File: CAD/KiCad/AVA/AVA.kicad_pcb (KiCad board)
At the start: 2 copper layers, 100 x 75 mm, 48 parts, among them J1 Conn_01x03_Pin, J10 Conn_01x04_Pin, J2 Conn_01x03_Pin, J3 Conn_01x03_Pin, J4 Conn_01x03_Pin, J5 Conn_01x02_Pin, J6 Conn_01x02_Pin, J7 Conn_01x02_Pin, J8 Conn_01x03_Pin, J9 Conn_01x03_Pin, U1 ESP32-C3-Super-Mini, U2 ESP32-DevKitC

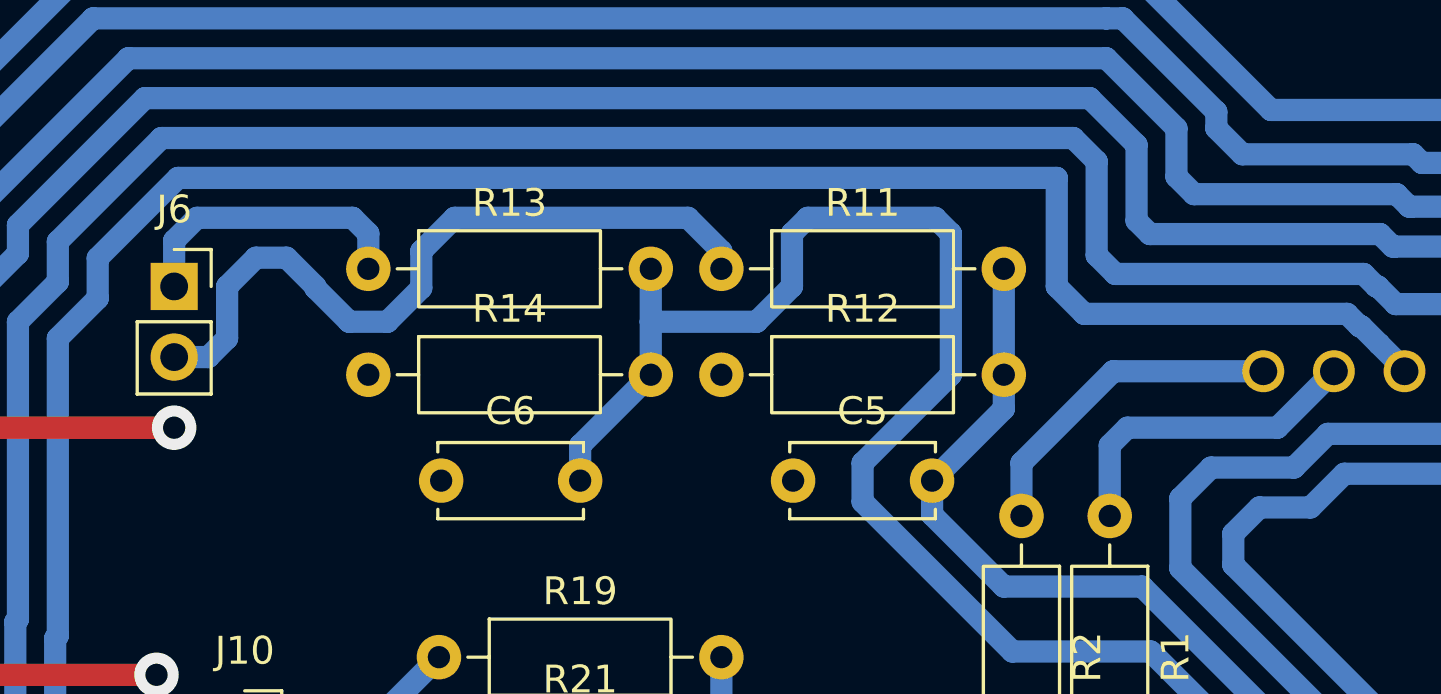
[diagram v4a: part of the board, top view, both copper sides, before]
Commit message: Added edges to Cu-Edit
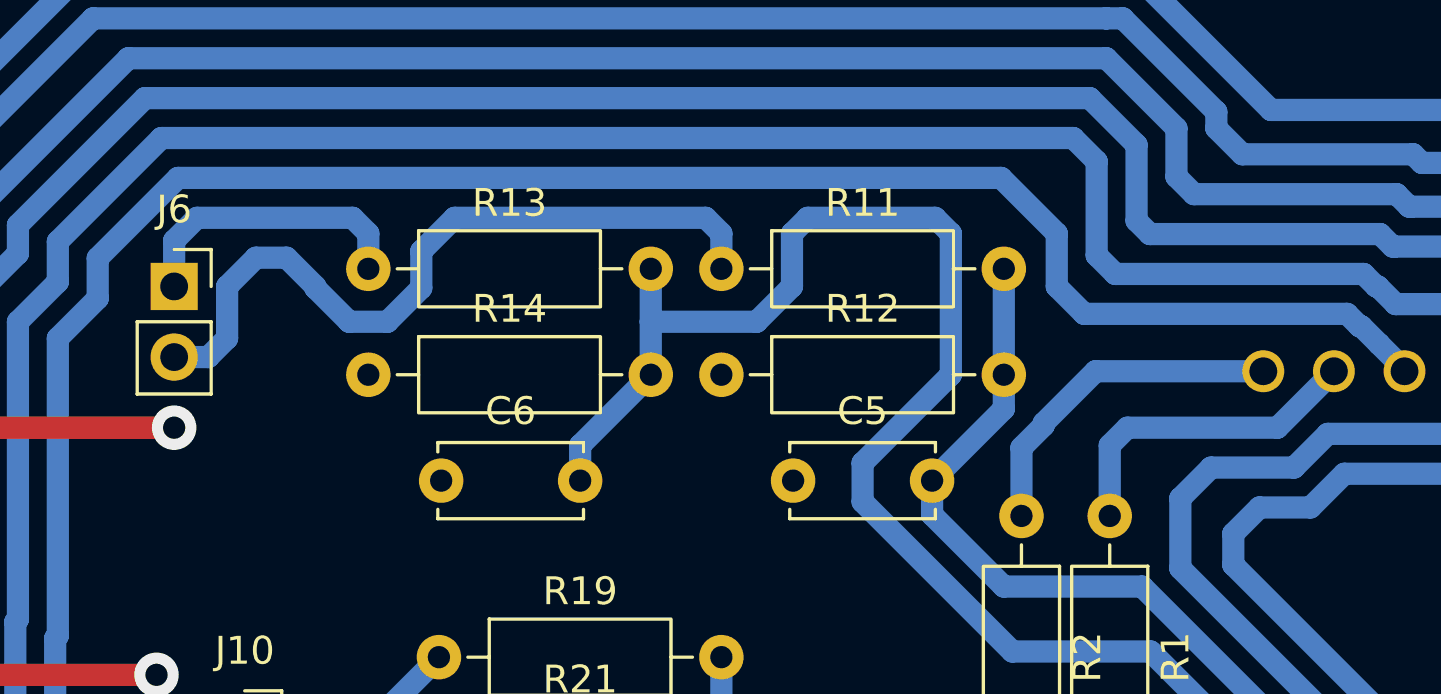
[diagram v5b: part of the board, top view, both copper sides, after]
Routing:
- net Net-(U1-GPIO10): track 88.1 -> 86.9 mm
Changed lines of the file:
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@@
+	)
+	(segment
+		(start 192.405 61.595)
+		(end 192.405 63.5)
+		(width 0.8)
+		(layer "B.Cu")
+		(net "Net-(U1-GPIO10)")
+	)
+	(segment
+		(start 203.999999 65.569999)
+		(end 204.915 66.485)
+		(width 0.8)
+		(layer "B.Cu")
+		(net "Net-(U1-GPIO10)")
+	)
+	(segment
+		(start 156.47 65.364396)
+		(end 157.904998 63.929398)
+		(width 0.8)
+		(layer "B.Cu")
+		(net "Net-(U1-GPIO10)")
+	)
+	(segment
+		(start 151.765 94.615)
+		(end 153.732198 92.647802)
+		(width 0.8)
+		(layer "B.Cu")
+		(net "Net-(U1-GPIO10)")
+	)
+	(segment
+		(start 202.85 64.485)
+		(end 203.3 64.935)
+		(width 0.8)
+		(layer "B.Cu")
+		(net "Net-(U1-GPIO10)")
+	)
+	(segment
+		(start 157.904998 63.929398)
+		(end 157.904998 62.480002)
+		(width 0.8)
+		(layer "B.Cu")
+		(net "Net-(U1-GPIO10)")
+	)
+	(segment
+		(start 156.375 76.159396)
+		(end 156.469999 76.064397)
+		(width 0.8)
+		(layer "B.Cu")
+		(net "Net-(U1-GPIO10)")
 	)
 	(segment
@@
 	)
 	(segment
+		(start 153.732198 92.647802)
+		(end 153.732198 85.787198)
+		(width 0.8)
+		(layer "B.Cu")
+		(net "Net-(U1-GPIO10)")
+	)
+	(segment
 		(start 160.79 59.595)
-		(end 192.405 59.595)
-		(width 0.8)
-		(layer "B.Cu")
-		(net "Net-(U1-GPIO10)")
-	)
-	(segment
-		(start 157.904998 63.929398)
-		(end 157.904998 62.480002)
-		(width 0.8)
-		(layer "B.Cu")
-		(net "Net-(U1-GPIO10)")
-	)
-	(segment
-		(start 203.999999 65.569999)
-		(end 204.915 66.485)
-		(width 0.8)
-		(layer "B.Cu")
-		(net "Net-(U1-GPIO10)")
-	)
-	(segment
-		(start 151.765 94.615)
-		(end 153.732198 92.647802)
+		(end 190.405 59.595)
+		(width 0.8)
+		(layer "B.Cu")
+		(net "Net-(U1-GPIO10)")
+	)
+	(segment
+		(start 190.405 59.595)
+		(end 192.405 61.595)
+		(width 0.8)
+		(layer "B.Cu")
+		(net "Net-(U1-GPIO10)")
+	)
+	(segment
+		(start 204.915 66.485)
+		(end 204.915 66.55)
+		(width 0.8)
+		(layer "B.Cu")
+		(net "Net-(U1-GPIO10)")
+	)
+	(segment
+		(start 192.405 63.5)
+		(end 193.39 64.485)
+		(width 0.8)
+		(layer "B.Cu")
+		(net "Net-(U1-GPIO10)")
+	)
+	(segment
+		(start 203.3 64.935)
+		(end 203.364986 64.934999)
+		(width 0.8)
+		(layer "B.Cu")
+		(net "Net-(U1-GPIO10)")
+	)
+	(segment
+		(start 156.375 83.144396)
+		(end 156.375 76.159396)
+		(width 0.8)
+		(layer "B.Cu")
+		(net "Net-(U1-GPIO10)")
+	)
+	(segment
+		(start 203.364986 64.934999)
+		(end 203.999987 65.57)
+		(width 0.8)
+		(layer "B.Cu")
+		(net "Net-(U1-GPIO10)")
+	)
+	(segment
+		(start 157.904998 62.480002)
+		(end 160.79 59.595)
+		(width 0.8)
+		(layer "B.Cu")
+		(net "Net-(U1-GPIO10)")
+	)
+	(segment
+		(start 203.999987 65.57)
+		(end 203.999999 65.569999)
 		(width 0.8)
 		(layer "B.Cu")
@@
 	)
 	(segment
-		(start 153.732198 92.647802)
-		(end 153.732198 85.787198)
-		(width 0.8)
-		(layer "B.Cu")
-		(net "Net-(U1-GPIO10)")
-	)
-	(segment
-		(start 203.364986 64.934999)
-		(end 203.999987 65.57)
-		(width 0.8)
-		(layer "B.Cu")
-		(net "Net-(U1-GPIO10)")
-	)
-	(segment
-		(start 203.999987 65.57)
-		(end 203.999999 65.569999)
-		(width 0.8)
-		(layer "B.Cu")
-		(net "Net-(U1-GPIO10)")
-	)
-	(segment
 		(start 156.469999 76.064397)
 		(end 156.47 65.364396)
@@
 	)
 	(segment
-		(start 156.47 65.364396)
-		(end 157.904998 63.929398)
-		(width 0.8)
-		(layer "B.Cu")
-		(net "Net-(U1-GPIO10)")
-	)
-	(segment
-		(start 203.3 64.935)
-		(end 203.364986 64.934999)
-		(width 0.8)
-		(layer "B.Cu")
-		(net "Net-(U1-GPIO10)")
-	)
-	(segment
-		(start 156.375 76.159396)
-		(end 156.469999 76.064397)
-		(width 0.8)
-		(layer "B.Cu")
-		(net "Net-(U1-GPIO10)")
-	)
-	(segment
-		(start 204.915 66.485)
-		(end 204.915 66.55)
-		(width 0.8)
-		(layer "B.Cu")
-		(net "Net-(U1-GPIO10)")
-	)
-	(segment
-		(start 157.904998 62.480002)
-		(end 160.79 59.595)
-		(width 0.8)
-		(layer "B.Cu")
-		(net "Net-(U1-GPIO10)")
-	)
-	(segment
-		(start 192.405 59.595)
-		(end 192.405 63.5)
-		(width 0.8)
-		(layer "B.Cu")
-		(net "Net-(U1-GPIO10)")
-	)
-	(segment
-		(start 192.405 63.5)
-		(end 193.39 64.485)
-		(width 0.8)
-		(layer "B.Cu")
-		(net "Net-(U1-GPIO10)")
-	)
-	(segment
-		(start 202.85 64.485)
-		(end 203.3 64.935)
-		(width 0.8)
-		(layer "B.Cu")
-		(net "Net-(U1-GPIO10)")
-	)
-	(segment
-		(start 156.375 83.144396)
-		(end 156.375 76.159396)
-		(width 0.8)
-		(layer "B.Cu")
-		(net "Net-(U1-GPIO10)")
-	)
-	(segment
-		(start 191.135 69.85)
-		(end 194.435 66.55)
+		(start 191.935 68.499396)
+		(end 191.934999 68.415001)
 		(width 0.8)
 		(layer "B.Cu")
@@
 	)
 	(segment
+		(start 193.8 66.55)
+		(end 199.835 66.55)
+		(width 0.8)
+		(layer "B.Cu")
+		(net "Net-(U1-TX{slash}GPIO21)")
+	)
+	(segment
 		(start 191.135 71.755)
-		(end 191.135 69.85)
+		(end 191.135 69.299396)
 		(width 0.8)
 		(layer "B.Cu")
@@
 	)
 	(segment
-		(start 194.435 66.55)
-		(end 199.835 66.55)
+		(start 191.135 69.299396)
+		(end 191.935 68.499396)
+		(width 0.8)
+		(layer "B.Cu")
+		(net "Net-(U1-TX{slash}GPIO21)")
+	)
+	(segment
+		(start 191.934999 68.415001)
+		(end 193.8 66.55)
 		(width 0.8)
 		(layer "B.Cu")
@@
 	)
 	(segment
+		(start 180.34 61.595)
+		(end 180.34 62.865)
+		(width 0.8)
+		(layer "B.Cu")
+		(net "/BAT2(8V)")
+	)
+	(segment
+		(start 179.775 61.03)
+		(end 180.34 61.595)
+		(width 0.8)
+		(layer "B.Cu")
+		(net "/BAT2(8V)")
+	)
+	(segment
+		(start 160.655 66.04)
+		(end 161.885 66.04)
+		(width 0.8)
+		(layer "B.Cu")
+		(net "/BAT2(8V)")
+	)
+	(segment
 		(start 170.745 61.03)
-		(end 179.14 61.03)
+		(end 179.775 61.03)
+		(width 0.8)
+		(layer "B.Cu")
+		(net "/BAT2(8V)")
+	)
+	(segment
+		(start 169.545 62.23)
+		(end 170.745 61.03)
+		(width 0.8)
+		(layer "B.Cu")
+		(net "/BAT2(8V)")
+	)
+	(segment
+		(start 166.949918 64.77)
+		(end 168.330082 64.77)
+		(width 0.8)
+		(layer "B.Cu")
+		(net "/BAT2(8V)")
+	)
+	(segment
+		(start 165.735 63.5)
+		(end 165.735 63.555082)
+		(width 0.8)
+		(layer "B.Cu")
+		(net "/BAT2(8V)")
+	)
+	(segment
+		(start 161.885 66.04)
+		(end 162.56 65.365)
+		(width 0.8)
+		(layer "B.Cu")
+		(net "/BAT2(8V)")
+	)
+	(segment
+		(start 165.735 63.555082)
+		(end 166.949918 64.77)
+		(width 0.8)
+		(layer "B.Cu")
+		(net "/BAT2(8V)")
+	)
+	(segment
+		(start 162.56 65.365)
+		(end 162.56 63.5)
+		(width 0.8)
+		(layer "B.Cu")
+		(net "/BAT2(8V)")
+	)
+	(segment
+		(start 162.56 63.5)
+		(end 163.595 62.465)
 		(width 0.8)
 		(layer "B.Cu")
@@
 	)
 	(segment
-		(start 162.56 65.365)
-		(end 162.56 63.5)
-		(width 0.8)
-		(layer "B.Cu")
-		(net "/BAT2(8V)")
-	)
-	(segment
 		(start 164.7 62.465)
 		(end 165.735 63.5)
@@
 	)
 	(segment
-		(start 165.735 63.5)
-		(end 165.735 63.555082)
-		(width 0.8)
-		(layer "B.Cu")
-		(net "/BAT2(8V)")
-	)
-	(segment
-		(start 160.655 66.04)
-		(end 161.885 66.04)
-		(width 0.8)
-		(layer "B.Cu")
-		(net "/BAT2(8V)")
-	)
-	(segment
-		(start 162.56 63.5)
-		(end 163.595 62.465)
-		(width 0.8)
-		(layer "B.Cu")
-		(net "/BAT2(8V)")
-	)
-	(segment
-		(start 166.949918 64.77)
-		(end 168.330082 64.77)
-		(width 0.8)
-		(layer "B.Cu")
-		(net "/BAT2(8V)")
-	)
-	(segment
-		(start 161.885 66.04)
-		(end 162.56 65.365)
-		(width 0.8)
-		(layer "B.Cu")
-		(net "/BAT2(8V)")
-	)
-	(segment
-		(start 180.34 62.23)
-		(end 180.34 62.865)
-		(width 0.8)
-		(layer "B.Cu")
-		(net "/BAT2(8V)")
-	)
-	(segment
 		(start 163.595 62.465)
 		(end 164.7 62.465)
 		(width 0.8)
 		(layer "B.Cu")
-		(net "/BAT2(8V)")
-	)
-	(segment
-		(start 179.14 61.03)
-		(end 180.34 62.23)
-		(width 0.8)
-		(layer "B.Cu")
-		(net "/BAT2(8V)")
-	)
-	(segment
-		(start 169.545 62.23)
-		(end 170.745 61.03)
-		(width 0.8)
-		(layer "B.Cu")
-		(net "/BAT2(8V)")
-	)
-	(segment
-		(start 165.735 63.555082)
-		(end 166.949918 64.77)
-		(width 0.8)
-		(layer "B.Cu")
